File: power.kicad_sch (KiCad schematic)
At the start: 10 parts, among them U19 SN74ALS04 (КР1533ЛН1), U21 SN74ALS14 (КР1533ТЛ2), U39 IN74ALS32N (КР1533ЛЛ1), U40 IN74ALS00N (КР1533ЛА3), U75 IN74ALS32N (КР1533ЛЛ1)

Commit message: March 22nd additions
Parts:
- removed C? (x5): 0.1µF, Capacitor_SMD:C_0805_2012Metric, symbol Device:C
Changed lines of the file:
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@@
     (comment 2 "Евстафьев")
   )
-  (junction (at 80.645 54.61) (diameter 0) (color 0 0 0 0)
-  )
-  (junction (at 98.425 54.61) (diameter 0) (color 0 0 0 0)
-  )
-  (junction (at 45.72 29.21) (diameter 0) (color 0 0 0 0)
-  )
   (junction (at 72.39 54.61) (diameter 0) (color 0 0 0 0)
   )
   (junction (at 37.465 29.21) (diameter 0) (color 0 0 0 0)
   )
-  (junction (at 45.72 54.61) (diameter 0) (color 0 0 0 0)
-  )
-  (junction (at 107.95 54.61) (diameter 0) (color 0 0 0 0)
-  )
   (junction (at 29.845 57.15) (diameter 0) (color 0 0 0 0)
   )
@@
   (junction (at 54.61 29.21) (diameter 0) (color 0 0 0 0)
   )
-  (junction (at 98.425 29.21) (diameter 0) (color 0 0 0 0)
-  )
-  (junction (at 107.95 29.21) (diameter 0) (color 0 0 0 0)
-  )
   (junction (at 31.75 27.94) (diameter 0) (color 0 0 0 0)
   )
-  (junction (at 63.5 54.61) (diameter 0) (color 0 0 0 0)
-  )
   (junction (at 72.39 29.21) (diameter 0) (color 0 0 0 0)
   )
-  (junction (at 63.5 29.21) (diameter 0) (color 0 0 0 0)
-  )
-  (junction (at 80.645 29.21) (diameter 0) (color 0 0 0 0)
-  )
   (junction (at 89.535 29.21) (diameter 0) (color 0 0 0 0)
   )
   (junction (at 37.465 54.61) (diameter 0) (color 0 0 0 0)
   )
-  (wire (pts (xy 98.425 29.21) (xy 107.95 29.21))
-    (stroke (width 0) (type default) (color 0 0 0 0))
-  )
-  (wire (pts (xy 119.38 45.72) (xy 119.38 54.61))
-    (stroke (width 0) (type default) (color 0 0 0 0))
-  )
-  (wire (pts (xy 119.38 38.1) (xy 119.38 29.21))
-    (stroke (width 0) (type default) (color 0 0 0 0))
-  )
-  (wire (pts (xy 98.425 54.61) (xy 89.535 54.61))
-    (stroke (width 0) (type default) (color 0 0 0 0))
-  )
-  (wire (pts (xy 45.72 29.21) (xy 54.61 29.21))
-    (stroke (width 0) (type default) (color 0 0 0 0))
-  )
-  (wire (pts (xy 63.5 38.1) (xy 63.5 29.21))
-    (stroke (width 0) (type default) (color 0 0 0 0))
-  )
-  (wire (pts (xy 37.465 29.21) (xy 45.72 29.21))
-    (stroke (width 0) (type default) (color 0 0 0 0))
-  )
-  (wire (pts (xy 119.38 29.21) (xy 107.95 29.21))
+  (wire (pts (xy 89.535 29.21) (xy 107.95 29.21))
+    (stroke (width 0) (type default) (color 0 0 0 0))
+  )
+  (wire (pts (xy 89.535 54.61) (xy 107.95 54.61))
+    (stroke (width 0) (type default) (color 0 0 0 0))
+  )
+  (wire (pts (xy 37.465 29.21) (xy 54.61 29.21))
     (stroke (width 0) (type default) (color 0 0 0 0))
   )
@@
     (stroke (width 0) (type default) (color 0 0 0 0))
   )
-  (wire (pts (xy 80.645 45.72) (xy 80.645 54.61))
-    (stroke (width 0) (type default) (color 0 0 0 0))
-  )
   (wire (pts (xy 26.67 27.94) (xy 31.75 27.94))
     (stroke (width 0) (type default) (color 0 0 0 0))
   )
-  (wire (pts (xy 54.61 29.21) (xy 63.5 29.21))
-    (stroke (width 0) (type default) (color 0 0 0 0))
-  )
-  (wire (pts (xy 119.38 54.61) (xy 107.95 54.61))
-    (stroke (width 0) (type default) (color 0 0 0 0))
-  )
   (wire (pts (xy 31.75 27.94) (xy 37.465 27.94))
     (stroke (width 0) (type default) (color 0 0 0 0))
   )
-  (wire (pts (xy 45.72 54.61) (xy 54.61 54.61))
+  (wire (pts (xy 37.465 54.61) (xy 54.61 54.61))
     (stroke (width 0) (type default) (color 0 0 0 0))
   )
@@
     (stroke (width 0) (type default) (color 0 0 0 0))
   )
-  (wire (pts (xy 37.465 54.61) (xy 45.72 54.61))
-    (stroke (width 0) (type default) (color 0 0 0 0))
-  )
-  (wire (pts (xy 80.645 54.61) (xy 89.535 54.61))
-    (stroke (width 0) (type default) (color 0 0 0 0))
-  )
-  (wire (pts (xy 54.61 54.61) (xy 63.5 54.61))
-    (stroke (width 0) (type default) (color 0 0 0 0))
-  )
-  (wire (pts (xy 45.72 29.21) (xy 45.72 38.1))
-    (stroke (width 0) (type default) (color 0 0 0 0))
-  )
-  (wire (pts (xy 63.5 45.72) (xy 63.5 54.61))
-    (stroke (width 0) (type default) (color 0 0 0 0))
-  )
-  (wire (pts (xy 63.5 54.61) (xy 72.39 54.61))
-    (stroke (width 0) (type default) (color 0 0 0 0))
-  )
-  (wire (pts (xy 98.425 45.72) (xy 98.425 54.61))
-    (stroke (width 0) (type default) (color 0 0 0 0))
-  )
-  (wire (pts (xy 45.72 45.72) (xy 45.72 54.61))
-    (stroke (width 0) (type default) (color 0 0 0 0))
-  )
-  (wire (pts (xy 80.645 29.21) (xy 80.645 38.1))
-    (stroke (width 0) (type default) (color 0 0 0 0))
-  )
-  (wire (pts (xy 80.645 29.21) (xy 89.535 29.21))
-    (stroke (width 0) (type default) (color 0 0 0 0))
-  )
-  (wire (pts (xy 107.95 54.61) (xy 98.425 54.61))
-    (stroke (width 0) (type default) (color 0 0 0 0))
-  )
-  (wire (pts (xy 98.425 29.21) (xy 89.535 29.21))
+  (wire (pts (xy 54.61 54.61) (xy 72.39 54.61))
     (stroke (width 0) (type default) (color 0 0 0 0))
   )
@@
     (stroke (width 0) (type default) (color 0 0 0 0))
   )
-  (wire (pts (xy 63.5 29.21) (xy 72.39 29.21))
-    (stroke (width 0) (type default) (color 0 0 0 0))
-  )
-  (wire (pts (xy 98.425 38.1) (xy 98.425 29.21))
-    (stroke (width 0) (type default) (color 0 0 0 0))
-  )
-  (wire (pts (xy 72.39 54.61) (xy 80.645 54.61))
+  (wire (pts (xy 54.61 29.21) (xy 72.39 29.21))
+    (stroke (width 0) (type default) (color 0 0 0 0))
+  )
+  (wire (pts (xy 72.39 54.61) (xy 89.535 54.61))
     (stroke (width 0) (type default) (color 0 0 0 0))
   )
@@
     (stroke (width 0) (type default) (color 0 0 0 0))
   )
-  (wire (pts (xy 72.39 29.21) (xy 80.645 29.21))
+  (wire (pts (xy 72.39 29.21) (xy 89.535 29.21))
     (stroke (width 0) (type default) (color 0 0 0 0))
   )
@@
     )
     (pin "1")
-  )
-  (symbol (lib_id "Device:C") (at 119.38 41.91 0) (unit 1)
-    (in_bom yes) (on_board yes) (fields_autoplaced)
-    (property "Reference" "C?" (id 0) (at 123.19 40.6399 0)
-      (effects (font (size 1.27 1.27)) (justify left))
-    )
-    (property "Value" "0.1µF" (id 1) (at 123.19 43.1799 0)
-      (effects (font (size 1.27 1.27)) (justify left))
-    )
-    (property "Footprint" "Capacitor_SMD:C_0805_2012Metric" (id 2) (at 120.3452 45.72 0)
-      (effects (font (size 1.27 1.27)) hide)
-    )
-    (property "Datasheet" "~" (id 3) (at 119.38 41.91 0)
-      (effects (font (size 1.27 1.27)) hide)
-    )
-    (pin "1")
-    (pin "2")
   )
   (symbol (lib_id "74xx:74LS14") (at 107.95 41.91 0) (unit 7)
@@
     (pin "1")
   )
-  (symbol (lib_id "Device:C") (at 45.72 41.91 0) (unit 1)
-    (in_bom yes) (on_board yes) (fields_autoplaced)
-    (property "Reference" "C?" (id 0) (at 49.53 40.6399 0)
-      (effects (font (size 1.27 1.27)) (justify left))
-    )
-    (property "Value" "0.1µF" (id 1) (at 49.53 43.1799 0)
-      (effects (font (size 1.27 1.27)) (justify left))
-    )
-    (property "Footprint" "Capacitor_SMD:C_0805_2012Metric" (id 2) (at 46.6852 45.72 0)
-      (effects (font (size 1.27 1.27)) hide)
-    )
-    (property "Datasheet" "~" (id 3) (at 45.72 41.91 0)
-      (effects (font (size 1.27 1.27)) hide)
-    )
-    (pin "1")
-    (pin "2")
-  )
-  (symbol (lib_id "Device:C") (at 80.645 41.91 0) (unit 1)
-    (in_bom yes) (on_board yes) (fields_autoplaced)
-    (property "Reference" "C?" (id 0) (at 84.455 40.6399 0)
-      (effects (font (size 1.27 1.27)) (justify left))
-    )
-    (property "Value" "0.1µF" (id 1) (at 84.455 43.1799 0)
-      (effects (font (size 1.27 1.27)) (justify left))
-    )
-    (property "Footprint" "Capacitor_SMD:C_0805_2012Metric" (id 2) (at 81.6102 45.72 0)
-      (effects (font (size 1.27 1.27)) hide)
-    )
-    (property "Datasheet" "~" (id 3) (at 80.645 41.91 0)
-      (effects (font (size 1.27 1.27)) hide)
-    )
-    (pin "1")
-    (pin "2")
-  )
-  (symbol (lib_id "Device:C") (at 63.5 41.91 0) (unit 1)
-    (in_bom yes) (on_board yes) (fields_autoplaced)
-    (property "Reference" "C?" (id 0) (at 67.31 40.6399 0)
-      (effects (font (size 1.27 1.27)) (justify left))
-    )
-    (property "Value" "0.1µF" (id 1) (at 67.31 43.1799 0)
-      (effects (font (size 1.27 1.27)) (justify left))
-    )
-    (property "Footprint" "Capacitor_SMD:C_0805_2012Metric" (id 2) (at 64.4652 45.72 0)
-      (effects (font (size 1.27 1.27)) hide)
-    )
-    (property "Datasheet" "~" (id 3) (at 63.5 41.91 0)
-      (effects (font (size 1.27 1.27)) hide)
-    )
-    (pin "1")
-    (pin "2")
-  )
-  (symbol (lib_id "Device:C") (at 98.425 41.91 0) (unit 1)
-    (in_bom yes) (on_board yes) (fields_autoplaced)
-    (property "Reference" "C?" (id 0) (at 102.235 40.6399 0)
-      (effects (font (size 1.27 1.27)) (justify left))
-    )
-    (property "Value" "0.1µF" (id 1) (at 102.235 43.1799 0)
-      (effects (font (size 1.27 1.27)) (justify left))
-    )
-    (property "Footprint" "Capacitor_SMD:C_0805_2012Metric" (id 2) (at 99.3902 45.72 0)
-      (effects (font (size 1.27 1.27)) hide)
-    )
-    (property "Datasheet" "~" (id 3) (at 98.425 41.91 0)
-      (effects (font (size 1.27 1.27)) hide)
-    )
-    (pin "1")
-    (pin "2")
-  )
 )

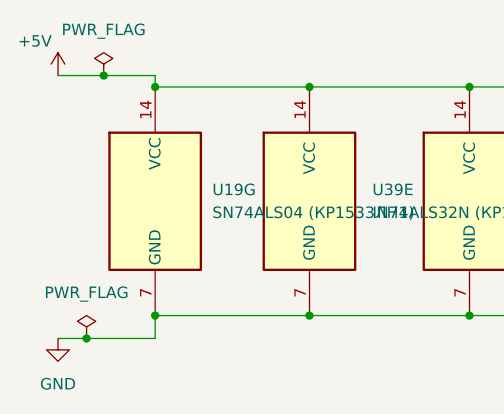
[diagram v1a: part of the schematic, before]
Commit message: March 23rd First pre-alpha
First time ZERO errors and 93 warnings. Schematics are done, now to deal with warnings and footprints.
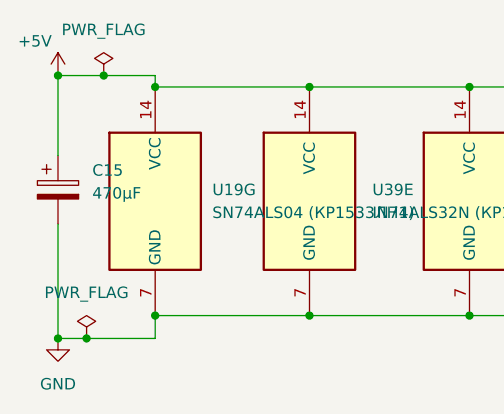
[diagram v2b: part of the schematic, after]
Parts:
- added C15: 470µF, Capacitor_THT:CP_Radial_D10.0mm_P5.00mm, symbol Device:C_Polarized
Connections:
- net +5V: now also C15.1
- net GND: now also C15.2
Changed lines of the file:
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@@
     (comment 2 "Евстафьев")
   )
+  (junction (at 26.67 27.94) (diameter 0) (color 0 0 0 0)
+  )
   (junction (at 72.39 54.61) (diameter 0) (color 0 0 0 0)
   )
@@
   (junction (at 72.39 29.21) (diameter 0) (color 0 0 0 0)
   )
+  (junction (at 26.67 57.15) (diameter 0) (color 0 0 0 0)
+  )
   (junction (at 89.535 29.21) (diameter 0) (color 0 0 0 0)
   )
@@
     (stroke (width 0) (type default) (color 0 0 0 0))
   )
+  (wire (pts (xy 26.67 44.45) (xy 26.67 57.15))
+    (stroke (width 0) (type default) (color 0 0 0 0))
+  )
   (wire (pts (xy 89.535 54.61) (xy 107.95 54.61))
     (stroke (width 0) (type default) (color 0 0 0 0))
@@
   )
   (wire (pts (xy 29.845 57.15) (xy 37.465 57.15))
+    (stroke (width 0) (type default) (color 0 0 0 0))
+  )
+  (wire (pts (xy 26.67 27.94) (xy 26.67 36.83))
     (stroke (width 0) (type default) (color 0 0 0 0))
   )
@@
     (pin "1")
   )
+  (symbol (lib_id "Device:C_Polarized") (at 26.67 40.64 0) (unit 1)
+    (in_bom yes) (on_board yes) (fields_autoplaced)
+    (property "Reference" "C15" (id 0) (at 30.48 38.4809 0)
+      (effects (font (size 1.27 1.27)) (justify left))
+    )
+    (property "Value" "470µF" (id 1) (at 30.48 41.0209 0)
+      (effects (font (size 1.27 1.27)) (justify left))
+    )
+    (property "Footprint" "Capacitor_THT:CP_Radial_D10.0mm_P5.00mm" (id 2) (at 27.6352 44.45 0)
+      (effects (font (size 1.27 1.27)) hide)
+    )
+    (property "Datasheet" "~" (id 3) (at 26.67 40.64 0)
+      (effects (font (size 1.27 1.27)) hide)
+    )
+    (pin "1")
+    (pin "2")
+  )
 )

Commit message: March 26th update
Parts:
- U19, U21, U39, U40, U75: footprint Package_DIP:DIP-14_W7.62mm_Socket_LongPads -> Package_DIP:DIP-14_W7.62mm_Socket
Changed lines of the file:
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@@
       (effects (font (size 1.27 1.27)) (justify left))
     )
-    (property "Footprint" "Package_DIP:DIP-14_W7.62mm_Socket_LongPads" (id 2) (at 54.61 41.91 0)
+    (property "Footprint" "Package_DIP:DIP-14_W7.62mm_Socket" (id 2) (at 54.61 41.91 0)
       (effects (font (size 1.27 1.27)) hide)
     )
@@
       (effects (font (size 1.27 1.27)) (justify left))
     )
-    (property "Footprint" "Package_DIP:DIP-14_W7.62mm_Socket_LongPads" (id 2) (at 107.95 41.91 0)
+    (property "Footprint" "Package_DIP:DIP-14_W7.62mm_Socket" (id 2) (at 107.95 41.91 0)
       (effects (font (size 1.27 1.27)) hide)
     )
@@
       (effects (font (size 1.27 1.27)) (justify left))
     )
-    (property "Footprint" "Package_DIP:DIP-14_W7.62mm_Socket_LongPads" (id 2) (at 37.465 41.91 0)
+    (property "Footprint" "Package_DIP:DIP-14_W7.62mm_Socket" (id 2) (at 37.465 41.91 0)
       (effects (font (size 1.27 1.27)) hide)
     )
@@
       (effects (font (size 1.27 1.27)) (justify left))
     )
-    (property "Footprint" "Package_DIP:DIP-14_W7.62mm_Socket_LongPads" (id 2) (at 89.535 41.91 0)
+    (property "Footprint" "Package_DIP:DIP-14_W7.62mm_Socket" (id 2) (at 89.535 41.91 0)
       (effects (font (size 1.27 1.27)) hide)
     )
@@
       (effects (font (size 1.27 1.27)) (justify left))
     )
-    (property "Footprint" "Package_DIP:DIP-14_W7.62mm_Socket_LongPads" (id 2) (at 72.39 41.91 0)
+    (property "Footprint" "Package_DIP:DIP-14_W7.62mm_Socket" (id 2) (at 72.39 41.91 0)
       (effects (font (size 1.27 1.27)) hide)
     )

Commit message: March 31st Update
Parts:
- added C13, C16, C17, C18, C19, C2, C20, C23, C24, C29, C30, C31, C9: 0.1μF, Capacitor_THT:C_Disc_D7.0mm_W2.5mm_P5.00mm, symbol Device:C
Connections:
- net +5V: now also C13.1, C16.1, C17.1, C18.1, C19.1, C2.1, C20.1, C23.1, C24.1, C29.1, C30.1, C31.1, C9.1
- net GND: now also C13.2, C16.2, C17.2, C18.2, C19.2, C2.2, C20.2, C23.2, C24.2, C29.2, C30.2, C31.2, C9.2
